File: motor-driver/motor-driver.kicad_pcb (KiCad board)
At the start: 4 copper layers, 155 parts, among them J1 USB_B_Micro, J2 SM03B-SRSS-TB, J3 XT60PW-F, J4 B2B-PH-SM4-TB, Q10 NMOS, Q11 NMOS, Q12 NMOS, Q7 NMOS, Q8 NMOS, Q9 NMOS, SW1 SW_Push, SW2 SW_Push, U1 LM397, U10 W25Q128JVS, U11 DNF, U12 NCP1117-3.3_SOT223, U13 RP2350_80QFN, U2 LM397, U3 LM358DR, U4 LM397, U5 LM358DR, U6 LM358DR, U7 LM358DR, U8 LM358DR, U9 FAN7388, Y1 ABM8-272-T3

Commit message: commit before changing custom sullen key sense
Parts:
- removed the C15 at (219.0, 54.4)
- removed C8: 330uF, 330uFCap:CAPPRD500W60D1000H1400
- removed Q10, Q11, Q12, Q7, Q8, Q9: NMOS, IPD090N03L:DPAK228P998X235-3N
- added C1: 10uF, Capacitor_SMD:C_0603_1608Metric, B.Cu at (181.6, 101.9)
- added C14: 10uF, Capacitor_SMD:C_0603_1608Metric, B.Cu at (181.6, 103.5)
- added C15: 47uF, Capacitor_SMD:C_0603_1608Metric, F.Cu at (133.4, -18.2)
- added C15: 10uF, Capacitor_SMD:C_0603_1608Metric, B.Cu at (181.6, 105.1)
- added C42: 330uF, A768MS337M1VLAS022:CAPAE1030X1225N, B.Cu at (221.3, 60.3)
- added C44: 47uF, Capacitor_SMD:C_0201_0603Metric_Pad0.64x0.40mm_HandSolder, F.Cu at (122.4, -17.7)
- added C44: 10uF, Capacitor_SMD:C_0603_1608Metric, B.Cu at (181.6, 106.7)
- added C45: 10uF, Capacitor_SMD:C_0603_1608Metric, B.Cu at (170.0, 102.1)
- added C46: 10uF, Capacitor_SMD:C_0603_1608Metric, B.Cu at (170.0, 103.6)
- added C47: 10uF, Capacitor_SMD:C_0603_1608Metric, B.Cu at (170.0, 105.2)
- added C48: 10uF, Capacitor_SMD:C_0603_1608Metric, B.Cu at (170.0, 106.7)
- added C49: 10uF, Capacitor_SMD:C_0603_1608Metric, B.Cu at (156.2, 102.1)
- added C50: 10uF, Capacitor_SMD:C_0603_1608Metric, B.Cu at (156.2, 103.6)
- added C51: 10uF, Capacitor_SMD:C_0603_1608Metric, B.Cu at (156.2, 105.2)
- added C52: 10uF, Capacitor_SMD:C_0603_1608Metric, B.Cu at (156.2, 106.7)
- added MOSFET1: AON6512, AON6512:DFN5X6_8L_EP1_P_AOS, B.Cu at (161.7, 105.5)
- added MOSFET2: AON6512, AON6512:DFN5X6_8L_EP1_P_AOS, B.Cu at (156.5, 112.6)
- added MOSFET3: AON6512, AON6512:DFN5X6_8L_EP1_P_AOS, B.Cu at (174.9, 105.5)
- added MOSFET4: AON6512, AON6512:DFN5X6_8L_EP1_P_AOS, B.Cu at (186.4, 105.5)
- added MOSFET5: AON6512, AON6512:DFN5X6_8L_EP1_P_AOS, B.Cu at (169.1, 112.6)
- added MOSFET6: AON6512, AON6512:DFN5X6_8L_EP1_P_AOS, B.Cu at (181.7, 112.6)
- C10, C11, C12, C13, C16, C17, C18, C25, C39, C4, C5, C6, C7, C9: footprint Capacitor_SMD:C_0805_2012Metric -> Capacitor_SMD:C_0603_1608Metric
- C14: footprint Capacitor_SMD:C_0201_0603Metric_Pad0.64x0.40mm_HandSolder -> Capacitor_SMD:C_0603_1608Metric
- C19, C20, C21, C22: footprint Capacitor_SMD:C_0805_2012Metric -> Capacitor_SMD:C_0603_1608Metric; moved to B.Cu
- D1, D2, D3, U1, U2, U4, U9: moved to B.Cu
- R1, R10, R11, R12, R13, R14, R15, R16, R17, R18, R19, R2, R20, R21, R22, R23, R24, R25, R3, R37, R38, R39, R4, R40, R41, R42, R43, R44, R45, R46, R47, R48, R49, R5, R50, R51, R52, R53, R54, R58, R59, R60, R61, R62, R63, R64, R65, R7, R8, R9: footprint Resistor_SMD:R_0805_2012Metric -> Resistor_SMD:R_0603_1608Metric
- R26, R27, R28, R30, R31, R32, R33, R35, R36, R55, R56, R6, R72, R73, R74: footprint Resistor_SMD:R_0805_2012Metric -> Resistor_SMD:R_0603_1608Metric; moved to B.Cu
- moved R74 231.6 mm to (175.6, -67.6)
- moved C22 222.9 mm to (166.2, -69.5), turned to 0 degrees
- moved D3 221.8 mm to (172.1, -67.5)
- moved R72 215.6 mm to (152.3, -53.0), turned to 180 degrees
- moved R73 207.2 mm to (163.0, -44.0), turned to 0 degrees
- moved C19 205.3 mm to (166.6, -51.5), turned to 0 degrees
- moved C21 204.9 mm to (163.2, -51.5), turned to 180 degrees
- moved C20 204.2 mm to (158.6, -51.0), turned to -90 degrees
- moved D1 202.4 mm to (152.2, -49.5), turned to 180 degrees
- moved D2 200.6 mm to (163.1, -47.0), turned to 0 degrees
- moved R54 195.7 mm to (175.3, -52.0)
- moved R28 194.5 mm to (116.9, -36.0), turned to 180 degrees
- moved R41 193.7 mm to (179.9, -40.0), turned to 180 degrees
- moved R26 187.8 mm to (121.4, -36.9), turned to -90 degrees
- moved R43 185.7 mm to (132.4, -44.7), turned to 90 degrees
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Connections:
- J1 pad 1: VBUS -> unconnected-(J1-VBUS-Pad1)
- J4 pad 1: VBUS -> /RP2350/5V
- R59 pad 2: VBUS -> /RP2350/5V
- U12 pad 3: VBUS -> /RP2350/5V
- U3 pad 8: VBUS -> /RP2350/5V
- U5 pad 8: VBUS -> /RP2350/5V
- U6 pad 8: VBUS -> /RP2350/5V
- U7 pad 8: VBUS -> /RP2350/5V
- U8 pad 8: VBUS -> /RP2350/5V
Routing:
- net /current-sensing/W_CURRENT_SENSE_IN: vias 0 -> 4
- net /back-emf-sensing/V_BUS: vias 0 -> 13
- net /back-emf-sensing/MOTOR_GND: vias 0 -> 6
- added copper zone on In2.Cu, net +3V3
- added copper zone on In2.Cu, net /RP2350/5V
- added copper zone on B.Cu, net /back-emf-sensing/MOTOR_GND
- added copper zone on B.Cu, net /back-emf-sensing/U_LEG_COIL
- added copper zone on B.Cu, net /back-emf-sensing/V_BUS
- added copper zone on In2.Cu, net /back-emf-sensing/V_BUS
- added copper zone on B.Cu, net /back-emf-sensing/V_LEG_COIL
- added copper zone on B.Cu, net /back-emf-sensing/W_LEG_COIL
- added copper zone on B.Cu, net /current-sensing/U_CURRENT_SENSE_IN
- added copper zone on F.Cu, net /current-sensing/U_CURRENT_SENSE_IN
- added copper zone on B.Cu, net /current-sensing/V_CURRENT_SENSE_IN
- added copper zone on F.Cu, net /current-sensing/V_CURRENT_SENSE_IN
- added copper zone on B.Cu, net /current-sensing/W_CURRENT_SENSE_IN
- added copper zone on F.Cu, net /current-sensing/W_CURRENT_SENSE_IN
- added copper zone on In1.Cu, net GND
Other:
- board outline added: 40 x 82.4 mm

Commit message: routing complete
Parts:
- removed the C1 at (96.5, 51.2)
- removed the C1 at (181.6, 101.9)
- removed C10, C11, C12, C13, C16, C17, C18, C4, C5, C6, C7, C9: 1nF, Capacitor_SMD:C_0603_1608Metric
- removed the C14 at (144.4, -17.8)
- removed the C14 at (181.6, 103.5)
- removed the C15 at (133.4, -18.2)
- removed the C15 at (181.6, 105.1)
- removed C19: 1uF, Capacitor_SMD:C_0603_1608Metric
- removed C20, C21, C22: 0.1uF, Capacitor_SMD:C_0603_1608Metric
- removed C3: DNF, Capacitor_SMD:C_0402_1005Metric
- removed the C44 at (122.4, -17.7)
- removed the C44 at (181.6, 106.7)
- removed C45, C46, C47, C48, C49, C50, C51, C52: 10uF, Capacitor_SMD:C_0603_1608Metric
- removed D1, D2, D3: D_Schottky, Diode_SMD:D_0805_2012Metric
- removed L1: 100nH, Inductor_SMD:L_0805_2012Metric
- removed MOSFET3, MOSFET4, MOSFET5, MOSFET6: AON6512, AON6512:DFN5X6_8L_EP1_P_AOS
- removed R1, R10, R11, R12, R13, R2, R3, R4, R5, R7, R8, R9: 15k, Resistor_SMD:R_0603_1608Metric
- removed R14, R15, R16, R17, R18, R19: 20k, Resistor_SMD:R_0603_1608Metric
- removed R20, R21, R22, R23, R24, R25, R37, R38, R39, R40, R41, R42, R44, R45, R47, R48, R49, R50, R51, R52, R54, R58, R59, R63, R64, R65: 10k, Resistor_SMD:R_0603_1608Metric
- removed R43, R46, R53: 100k, Resistor_SMD:R_0603_1608Metric
- removed R60, R61, R62: 1k, Resistor_SMD:R_0603_1608Metric
- removed R72, R73, R74: 50, Resistor_SMD:R_0603_1608Metric
- removed R75, R77, R78, R79: DNF, Resistor_SMD:R_0402_1005Metric
- removed SW1, SW2: SW_Push, Button_Switch_SMD:SW_Push_1P1T_NO_Vertical_Wuerth_434133025816
- removed U11: DNF, Package_SO_new:SOIC-8_5.23x5.23mm_P1.27mm
- removed U2, U4: LM397, Package_TO_SOT_SMD:SOT-23-5
- removed U3, U5, U6, U7, U8: LM358DR, LM358DR:SOIC127P599X175-8N
- removed U9: FAN7388, Package_SO:SOIC-20W_7.5x12.8mm_P1.27mm
- added BOOT1: SW_Push, Button_Switch_SMD:SW_Push_1P1T_NO_Vertical_Wuerth_434133025816, F.Cu at (141.5, 59.2)
- added C1: 1uF, Capacitor_SMD:C_0603_1608Metric, F.Cu at (182.6, 83.3)
- added C14: 0.1uF, Capacitor_SMD:C_0603_1608Metric, F.Cu at (183.3, 72.5)
- added C15: 0.1uF, Capacitor_SMD:C_0603_1608Metric, F.Cu at (183.4, 77.9)
- added C43: 10uF, Capacitor_SMD:C_0603_1608Metric, F.Cu at (169.0, 94.2)
- added C44: 0.1uF, Capacitor_SMD:C_0603_1608Metric, F.Cu at (168.2, 81.9)
- added C53: 10uF, Capacitor_SMD:C_0603_1608Metric, F.Cu at (171.2, 94.2)
- added C54: 10uF, Capacitor_SMD:C_0603_1608Metric, F.Cu at (173.3, 94.2)
- added C55: 10uF, Capacitor_SMD:C_0603_1608Metric, F.Cu at (148.9, 93.9)
- added C56: 10uF, Capacitor_SMD:C_0603_1608Metric, F.Cu at (151.2, 93.9)
- added C57: 10uF, Capacitor_SMD:C_0603_1608Metric, F.Cu at (153.5, 93.9)
- added C58: 10uF, Capacitor_SMD:C_0603_1608Metric, F.Cu at (155.8, 93.9)
- added C59: 10uF, Capacitor_SMD:C_0603_1608Metric, F.Cu at (184.7, 93.8)
- added C60: 10uF, Capacitor_SMD:C_0603_1608Metric, F.Cu at (186.9, 93.8)
- added C61: 10uF, Capacitor_SMD:C_0603_1608Metric, F.Cu at (189.0, 93.8)
- added C62: 10uF, Capacitor_SMD:C_0603_1608Metric, F.Cu at (191.2, 93.8)
- added C8: 10uF, Capacitor_SMD:C_0603_1608Metric, F.Cu at (166.8, 94.2)
- added C_bypass1: 0.1uF, Capacitor_SMD:C_0603_1608Metric, F.Cu at (141.7, 101.2)
- added C_bypass2: 0.1uF, Capacitor_SMD:C_0603_1608Metric, F.Cu at (159.8, 101.5)
- added C_bypass3: 0.1uF, Capacitor_SMD:C_0603_1608Metric, F.Cu at (177.6, 101.5)
- added D4: D_Schottky, Diode_SMD:D_0805_2012Metric, F.Cu at (183.4, 69.1)
- added D5: D_Schottky, Diode_SMD:D_0805_2012Metric, F.Cu at (186.3, 77.1)
- added D6: D_Schottky, Diode_SMD:D_0805_2012Metric, F.Cu at (169.7, 84.9)
- added MOSFET10: AON6512, AON6512:DFN5X6_8L_EP1_P_AOS, F.Cu at (182.6, 101.8)
- added MOSFET7: AON6512, AON6512:DFN5X6_8L_EP1_P_AOS, F.Cu at (171.3, 101.8)
- added MOSFET8: AON6512, AON6512:DFN5X6_8L_EP1_P_AOS, F.Cu at (164.8, 101.8)
- added MOSFET9: AON6512, AON6512:DFN5X6_8L_EP1_P_AOS, F.Cu at (189.0, 101.8)
- added R100: 50, Resistor_SMD:R_0603_1608Metric, F.Cu at (169.8, 87.1)
- added R66: 22, Resistor_SMD:R_0603_1608Metric, F.Cu at (160.7, 96.3)
- added R67: 22, Resistor_SMD:R_0603_1608Metric, B.Cu at (173.4, 103.7)
- added R68: 10k, Resistor_SMD:R_0603_1608Metric, F.Cu at (173.4, 107.7)
- added R69: 10k, Resistor_SMD:R_0603_1608Metric, F.Cu at (159.8, 99.0)
- added R70: 5m, Resistor_SMD:R_2512_6332Metric, F.Cu at (164.1, 110.1)
- added R71: 22, Resistor_SMD:R_0603_1608Metric, F.Cu at (178.3, 96.3)
- added R86: 22, Resistor_SMD:R_0603_1608Metric, B.Cu at (190.8, 103.7)
- added R87: 10k, Resistor_SMD:R_0603_1608Metric, F.Cu at (191.4, 107.1)
- added R88: 10k, Resistor_SMD:R_0603_1608Metric, F.Cu at (177.8, 99.2)
- added R89: 5m, Resistor_SMD:R_2512_6332Metric, F.Cu at (182.2, 110.1)
- added R90: 10k, Resistor_SMD:R_0603_1608Metric, F.Cu at (159.6, 86.7)
- added R91: 10k, Resistor_SMD:R_0603_1608Metric, F.Cu at (163.5, 85.8)
- added R92: 10k, Resistor_SMD:R_0603_1608Metric, F.Cu at (158.4, 83.2)
- added R93: 1M, Resistor_SMD:R_0603_1608Metric, F.Cu at (164.2, 82.9)
- added R94: 10k, Resistor_SMD:R_0603_1608Metric, F.Cu at (163.2, 79.8)
- added R95: 10k, Resistor_SMD:R_0603_1608Metric, B.Cu at (149.6, 88.5)
- added R96: 10k, Resistor_SMD:R_0603_1608Metric, B.Cu at (151.2, 88.5)
- added R97: 10k, Resistor_SMD:R_0603_1608Metric, B.Cu at (152.8, 88.5)
- added R98: 50, Resistor_SMD:R_0603_1608Metric, F.Cu at (181.2, 68.7)
- added R99: 50, Resistor_SMD:R_0603_1608Metric, F.Cu at (186.4, 78.9)
- added RUN1: SW_Push, Button_Switch_SMD:SW_Push_1P1T_NO_Vertical_Wuerth_434133025816, F.Cu at (141.5, 66.9)
- added U14: LM397, Package_TO_SOT_SMD:SOT-23-5, F.Cu at (144.2, 83.4)
- added U15: LM397, Package_TO_SOT_SMD:SOT-23-5, F.Cu at (152.7, 83.0)
- added U16: LM397, Package_TO_SOT_SMD:SOT-23-5, F.Cu at (161.4, 82.9)
- added U17: FAN7388, Package_SO:SOIC-20W_7.5x12.8mm_P1.27mm, F.Cu at (175.8, 77.1)
- added U19: INA240A1PWR, INA240A1PWR:SOP65P640X120-8N, F.Cu at (141.5, 106.5)
- added U20: INA240A1PWR, INA240A1PWR:SOP65P640X120-8N, F.Cu at (159.5, 106.5)
- added U21: INA240A1PWR, INA240A1PWR:SOP65P640X120-8N, F.Cu at (177.6, 106.5)
- added V1: PAD, TestPoint:TestPoint_Pad_4.0x4.0mm, F.Cu at (169.3, 113.1)
- added W1: PAD, TestPoint:TestPoint_Pad_4.0x4.0mm, F.Cu at (187.4, 113.1)
- C26, C27: footprint Capacitor_SMD:C_0603_1608Metric -> Capacitor_SMD:C_0402_1005Metric
- C42, MOSFET1, MOSFET2, R27, R28, R30, R35: moved to F.Cu
- L2: footprint Inductor_SMD:L_0603_1608Metric -> Inductor_SMD:L_Cenker_CKCS201610
- R26, R31, R32, R36, R55: value 22 -> 10k; moved to F.Cu
- R33, R56: value 10k -> 1M; moved to F.Cu
- R34, R57: value 5m -> 10k; footprint Resistor_SMD:R_2512_6332Metric -> Resistor_SMD:R_0603_1608Metric
- R6: value 10k -> 22
- U1: value LM397 -> PAD; footprint Package_TO_SOT_SMD:SOT-23-5 -> TestPoint:TestPoint_Pad_4.0x4.0mm; moved to F.Cu
- moved H1 247.5 mm to (262.0, 86.5)
- moved H2 247.5 mm to (262.0, 93.4)
- moved H3 247.5 mm to (262.0, 100.3)
- moved H4 247.5 mm to (262.0, 107.3)
- moved J2 154.6 mm to (162.2, 73.1), turned to 0 degrees
- moved R26 148.2 mm to (155.6, 107.3), turned to 90 degrees
- moved R6 140.0 mm to (155.4, 103.3), turned to -90 degrees
- moved R28 137.3 mm to (141.8, 99.0), turned to 0 degrees
- moved R27 133.1 mm to (142.7, 96.3)
- moved R35 127.3 mm to (151.2, 86.9), turned to -90 degrees
- moved R30 124.4 mm to (142.4, 87.1), turned to -90 degrees
- moved R55 124.2 mm to (149.8, 83.6), turned to 90 degrees
- moved R36 124.0 mm to (154.6, 86.0), turned to 180 degrees
- moved R31 123.7 mm to (146.2, 86.3), turned to 180 degrees
- moved R32 122.0 mm to (141.4, 83.7), turned to 90 degrees
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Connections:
- C2 pad 1: +3V3 -> 3V3
- C25 pad 1: +3V3 -> 3V3
- C26 pad 1: +3V3 -> 3V3
- C32 pad 1: +3V3 -> 3V3
- C33 pad 1: +3V3 -> 3V3
- C34 pad 1: +3V3 -> 3V3
- C35 pad 1: +3V3 -> 3V3
- C36 pad 1: +3V3 -> 3V3
- C37 pad 1: +3V3 -> 3V3
- C38 pad 1: +3V3 -> 3V3
- C39 pad 1: +3V3 -> 3V3
- C40 pad 1: +3V3 -> 3V3
- C41 pad 1: +3V3 -> 3V3
- C42 pad 1: /back-emf-sensing/V_BUS -> V_BUS
- C42 pad 2: /back-emf-sensing/MOTOR_GND -> GND
- J1 pad 1: unconnected-(J1-VBUS-Pad1) -> 5V
- J3 pad 1: /back-emf-sensing/V_BUS -> V_BUS
- J3 pad 2: /back-emf-sensing/MOTOR_GND -> GND
- J4 pad 1: /RP2350/5V -> 5V
- J4 pad 2: /back-emf-sensing/MOTOR_GND -> GND
- MOSFET1 pad 1: /back-emf-sensing/U_LEG_COIL -> /inverter/inverter_u/SHUNT_P
- MOSFET1 pad 2: /back-emf-sensing/U_LEG_COIL -> /inverter/inverter_u/SHUNT_P
- MOSFET1 pad 3: /back-emf-sensing/U_LEG_COIL -> /inverter/inverter_u/SHUNT_P
- MOSFET1 pad 5: /back-emf-sensing/V_BUS -> V_BUS
- MOSFET1 pad 6: /back-emf-sensing/V_BUS -> V_BUS
- MOSFET1 pad 7: /back-emf-sensing/V_BUS -> V_BUS
- MOSFET1 pad 8: /back-emf-sensing/V_BUS -> V_BUS
- MOSFET2 pad 1: /current-sensing/U_CURRENT_SENSE_IN -> GND
- MOSFET2 pad 2: /current-sensing/U_CURRENT_SENSE_IN -> GND
- MOSFET2 pad 3: /current-sensing/U_CURRENT_SENSE_IN -> GND
- MOSFET2 pad 5: /back-emf-sensing/U_LEG_COIL -> /inverter/inverter_u/SHUNT_P
- MOSFET2 pad 6: /back-emf-sensing/U_LEG_COIL -> /inverter/inverter_u/SHUNT_P
- MOSFET2 pad 7: /back-emf-sensing/U_LEG_COIL -> /inverter/inverter_u/SHUNT_P
- MOSFET2 pad 8: /back-emf-sensing/U_LEG_COIL -> /inverter/inverter_u/SHUNT_P
- R26 pad 1: /gate-driver/U_LEG_HIGH -> GND
- R27 pad 1: /gate-driver/U_LEG_LOW -> /inverter/gate-driver/U_GATE_L
- R28 pad 1: /back-emf-sensing/MOTOR_GND -> GND
- R28 pad 2: Net-(MOSFET1-Pad4) -> Net-(MOSFET2-Pad4)
- R29 pad 1: /back-emf-sensing/MOTOR_GND -> /inverter/inverter_u/SHUNT_N
- R29 pad 2: /current-sensing/U_CURRENT_SENSE_IN -> /inverter/inverter_u/SHUNT_P
- R30 pad 1: /back-emf-sensing/MOTOR_GND -> Net-(U14--)
- R30 pad 2: Net-(MOSFET5-Pad4) -> /inverter/inverter_u/SHUNT_N
- R31 pad 1: /gate-driver/V_LEG_HIGH -> GND
- R31 pad 2: Net-(MOSFET3-Pad4) -> MOTOR_NEUTRAL_REF
- R32 pad 1: /inverter/V_LEG_LOW -> Net-(U14--)
- R32 pad 2: Net-(MOSFET5-Pad4) -> GND
- R33 pad 1: /back-emf-sensing/MOTOR_GND -> MOTOR_NEUTRAL_REF
- R33 pad 2: Net-(MOSFET3-Pad4) -> /RP2350/BACK_EMF_U
- R34 pad 1: /back-emf-sensing/MOTOR_GND -> 3V3
- R34 pad 2: /current-sensing/V_CURRENT_SENSE_IN -> /RP2350/BACK_EMF_U
- R35 pad 1: /back-emf-sensing/MOTOR_GND -> Net-(U15--)
- R35 pad 2: Net-(MOSFET6-Pad4) -> /inverter/inverter_v/SHUNT_N
- R36 pad 1: /gate-driver/W_LEG_HIGH -> GND
- R36 pad 2: Net-(MOSFET4-Pad4) -> MOTOR_NEUTRAL_REF
- R55 pad 1: /gate-driver/W_LEG_LOW -> Net-(U15--)
- R55 pad 2: Net-(MOSFET6-Pad4) -> GND
- R56 pad 1: /back-emf-sensing/MOTOR_GND -> MOTOR_NEUTRAL_REF
- R56 pad 2: Net-(MOSFET4-Pad4) -> /RP2350/BACK_EMF_V
- R57 pad 1: /back-emf-sensing/MOTOR_GND -> 3V3
- R57 pad 2: /current-sensing/W_CURRENT_SENSE_IN -> /RP2350/BACK_EMF_V
- R6 pad 1: /back-emf-sensing/MOTOR_GND -> /inverter/gate-driver/U_GATE_H
- R6 pad 2: Net-(MOSFET2-Pad4) -> Net-(MOSFET1-Pad4)
- R82 pad 1: +3V3 -> 3V3
- U1 pad 1: Net-(U1--) -> /inverter/inverter_u/SHUNT_N
- U10 pad 8: +3V3 -> 3V3
- U12 pad 2: +3V3 -> 3V3
- U12 pad 3: /RP2350/5V -> 5V
- U13 pad 1: /RP2350/PWM_U_H -> unconnected-(U13-GPIO4-Pad1)
- U13 pad 11: /RP2350/GPIO10 -> /RP2350/GPIO12
- U13 pad 12: /RP2350/GPIO10 -> /RP2350/GPIO13
- U13 pad 13: /RP2350/GPIO10 -> /RP2350/GPIO14
- U13 pad 14: /RP2350/GPIO10 -> /RP2350/GPIO15
- U13 pad 15: +3V3 -> 3V3
- U13 pad 16: /RP2350/GPIO10 -> /RP2350/GPIO16
- U13 pad 17: /RP2350/GPIO10 -> /RP2350/GPIO17
- U13 pad 18: /RP2350/GPIO10 -> /RP2350/GPIO18
- U13 pad 19: /RP2350/GPIO10 -> /RP2350/GPIO19
- U13 pad 2: /RP2350/PWM_U_L -> unconnected-(U13-GPIO5-Pad2)
- U13 pad 20: /RP2350/GPIO10 -> /RP2350/GPIO20
- U13 pad 21: /RP2350/GPIO10 -> /RP2350/BACK_EMF_U
- U13 pad 22: /RP2350/GPIO10 -> /RP2350/BACK_EMF_V
- U13 pad 23: /RP2350/GPIO10 -> /RP2350/BACK_EMF_W
- U13 pad 24: +3V3 -> 3V3
- U13 pad 25: /RP2350/GPIO10 -> /RP2350/GPIO24
- U13 pad 26: /RP2350/GPIO10 -> /RP2350/GPIO25
- U13 pad 27: /RP2350/GPIO10 -> /RP2350/GPIO26
- U13 pad 28: /RP2350/GPIO10 -> /RP2350/GPIO27
- U13 pad 29: +3V3 -> 3V3
- U13 pad 3: /RP2350/PWM_V_H -> unconnected-(U13-GPIO6-Pad3)
- U13 pad 36: /RP2350/GPIO10 -> /RP2350/PWM_U_L
- U13 pad 37: /RP2350/GPIO10 -> /RP2350/PWM_U_H
- U13 pad 38: /RP2350/GPIO10 -> /RP2350/PWM_V_L
- U13 pad 39: /RP2350/GPIO10 -> /RP2350/PWM_V_H
- U13 pad 4: /RP2350/PWM_V_L -> unconnected-(U13-GPIO7-Pad4)
- U13 pad 40: /RP2350/GPIO10 -> /RP2350/PWM_W_L
- U13 pad 41: +3V3 -> 3V3
- U13 pad 42: /RP2350/GPIO10 -> /RP2350/PWM_W_H
- U13 pad 43: /RP2350/GPIO10 -> /RP2350/GPIO34
- U13 pad 44: /RP2350/GPIO10 -> /RP2350/GPIO35
- U13 pad 45: /RP2350/GPIO10 -> /RP2350/GPIO36
- U13 pad 46: /RP2350/GPIO10 -> /RP2350/GPIO37
- U13 pad 47: /RP2350/GPIO10 -> /RP2350/GPIO38
- U13 pad 48: /RP2350/GPIO10 -> /RP2350/GPIO39
- U13 pad 49: /RP2350/CURRENT_SENSE_U -> unconnected-(U13-GPIO40_ADC0-Pad49)
- U13 pad 5: +3V3 -> 3V3
- U13 pad 50: +3V3 -> 3V3
- U13 pad 52: /RP2350/CURRENT_SENSE_V -> unconnected-(U13-GPIO41_ADC1-Pad52)
- U13 pad 53: /RP2350/CURRENT_SENSE_W -> unconnected-(U13-GPIO42_ADC2-Pad53)
- U13 pad 55: /RP2350/GPIO43_ADC3 -> /RP2350/CURRENT_SENSE_U
- U13 pad 56: /RP2350/GPIO43_ADC3 -> /RP2350/CURRENT_SENSE_V
- U13 pad 57: /RP2350/GPIO43_ADC3 -> /RP2350/CURRENT_SENSE_W
- U13 pad 58: /RP2350/GPIO43_ADC3 -> /RP2350/GPIO47_ADC7
- U13 pad 59: +3V3 -> 3V3
- U13 pad 6: /RP2350/PWM_W_H -> unconnected-(U13-GPIO8-Pad6)
- U13 pad 60: +3V3 -> 3V3
- U13 pad 64: +3V3 -> 3V3
- U13 pad 68: +3V3 -> 3V3
- U13 pad 69: +3V3 -> 3V3
- U13 pad 7: /RP2350/PWM_W_L -> unconnected-(U13-GPIO9-Pad7)
- U13 pad 76: +3V3 -> 3V3
- U13 pad 77: /RP2350/BACK_EMF_U -> unconnected-(U13-GPIO0-Pad77)
- U13 pad 78: /RP2350/BACK_EMF_V -> unconnected-(U13-GPIO1-Pad78)
- U13 pad 79: /RP2350/BACK_EMF_W -> unconnected-(U13-GPIO2-Pad79)
- U13 pad 9: /RP2350/GPIO10 -> /RP2350/GPIO11
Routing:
- net /inverter/inverter_w/SHUNT_N: track 0.00 -> 86.4 mm, vias 0 -> 2
- net /inverter/inverter_v/SHUNT_N: track 0.00 -> 67.8 mm, vias 0 -> 4
- net GND: track 0.00 -> 67.4 mm, vias 0 -> 90
- net /RP2350/CURRENT_SENSE_U: track 0.00 -> 62.6 mm, vias 0 -> 2
- net 3V3: track 0.00 -> 61.4 mm, vias 0 -> 18
- net /inverter/inverter_u/SHUNT_P: track 0.00 -> 57.5 mm, vias 0 -> 2
- net /RP2350/CURRENT_SENSE_W: track 0.00 -> 57.2 mm
- net /inverter/inverter_w/SHUNT_P: track 0.00 -> 57.0 mm, vias 0 -> 2
- net /inverter/inverter_v/SHUNT_P: track 0.00 -> 55.7 mm, vias 0 -> 2
- net /RP2350/CURRENT_SENSE_V: track 0.00 -> 50.4 mm, vias 0 -> 2
- net /inverter/inverter_u/SHUNT_N: track 0.00 -> 47.6 mm, vias 0 -> 2
- net /inverter/gate-driver/W_GATE_H: track 0.00 -> 40.4 mm, vias 0 -> 1
- net /inverter/gate-driver/U_GATE_L: track 0.00 -> 38.2 mm, vias 0 -> 2
- net /inverter/gate-driver/V_GATE_L: track 0.00 -> 37.7 mm, vias 0 -> 2
- net /RP2350/BACK_EMF_W: track 0.00 -> 34.8 mm
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- added copper zone on F.Cu, net +1V1
- added copper zone on F.Cu, net /RP2350/USB_D+
- added copper zone on F.Cu, net /RP2350/USB_D-
- added copper zone on F.Cu, net /RP2350/VREG_LX
- added copper zone on F.Cu, net /inverter/inverter_u/SHUNT_N
- added copper zone on F.Cu, net /inverter/inverter_u/SHUNT_P
- added copper zone on F.Cu, net /inverter/inverter_v/SHUNT_N
- added copper zone on F.Cu, net /inverter/inverter_v/SHUNT_P
- added copper zone on F.Cu, net /inverter/inverter_w/SHUNT_N
- added copper zone on F.Cu, net /inverter/inverter_w/SHUNT_P
- added copper zone on F.Cu, net 3V3
- added copper zone on In2.Cu, net 3V3
- added copper zone on F.Cu, net 5V
- added copper zone on F.Cu, net GND
- added copper zone on F.Cu, net V_BUS
- added copper zone on In2.Cu, net V_BUS
- removed copper zone on In2.Cu, net +3V3
- removed copper zone on In2.Cu, net /RP2350/5V
- removed copper zone on B.Cu, net /back-emf-sensing/MOTOR_GND
- removed copper zone on B.Cu, net /back-emf-sensing/U_LEG_COIL
- removed copper zone on B.Cu, net /back-emf-sensing/V_BUS
- removed copper zone on In2.Cu, net /back-emf-sensing/V_BUS
- removed copper zone on B.Cu, net /back-emf-sensing/V_LEG_COIL
- removed copper zone on B.Cu, net /back-emf-sensing/W_LEG_COIL
- removed copper zone on B.Cu, net /current-sensing/U_CURRENT_SENSE_IN
- removed copper zone on F.Cu, net /current-sensing/U_CURRENT_SENSE_IN
- removed copper zone on B.Cu, net /current-sensing/V_CURRENT_SENSE_IN
- removed copper zone on F.Cu, net /current-sensing/V_CURRENT_SENSE_IN
- removed copper zone on B.Cu, net /current-sensing/W_CURRENT_SENSE_IN
- removed copper zone on F.Cu, net /current-sensing/W_CURRENT_SENSE_IN
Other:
- board size 40 x 82.4 mm -> 56 x 85.4 mm

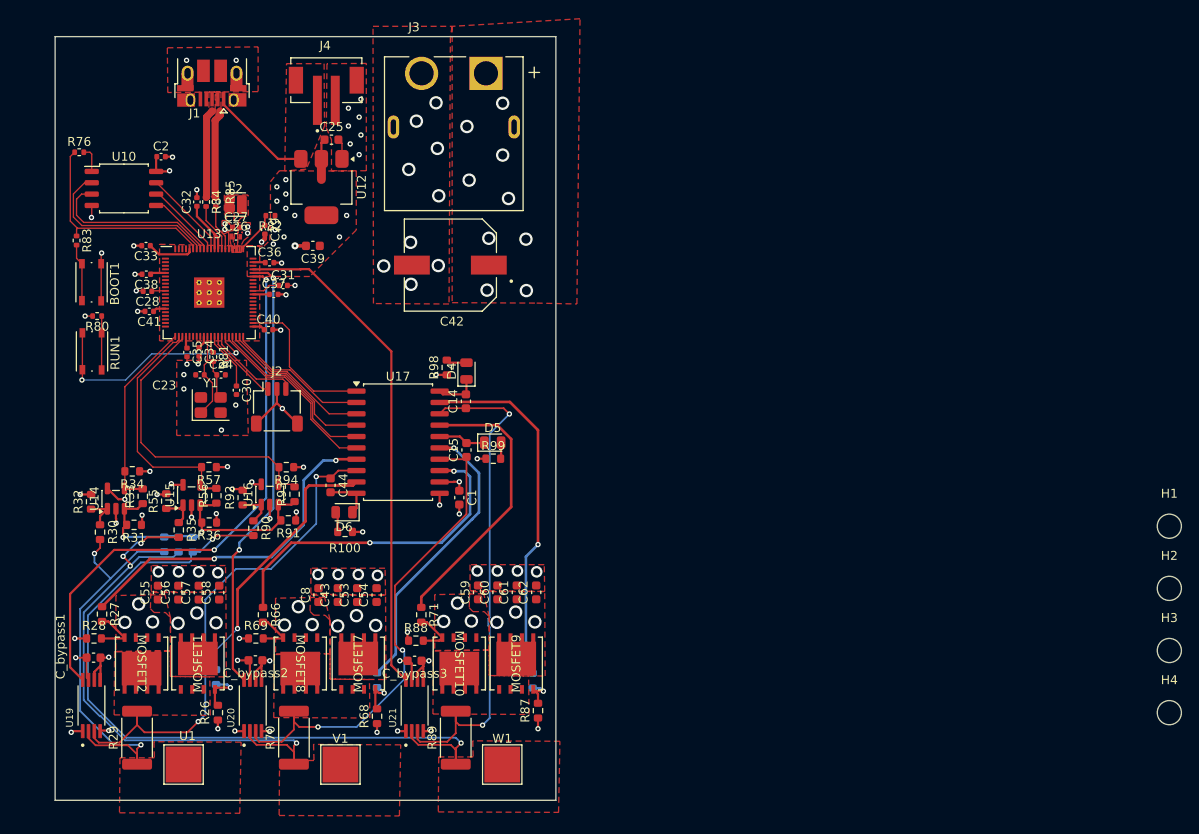
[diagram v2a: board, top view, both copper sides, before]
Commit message: added spi connection
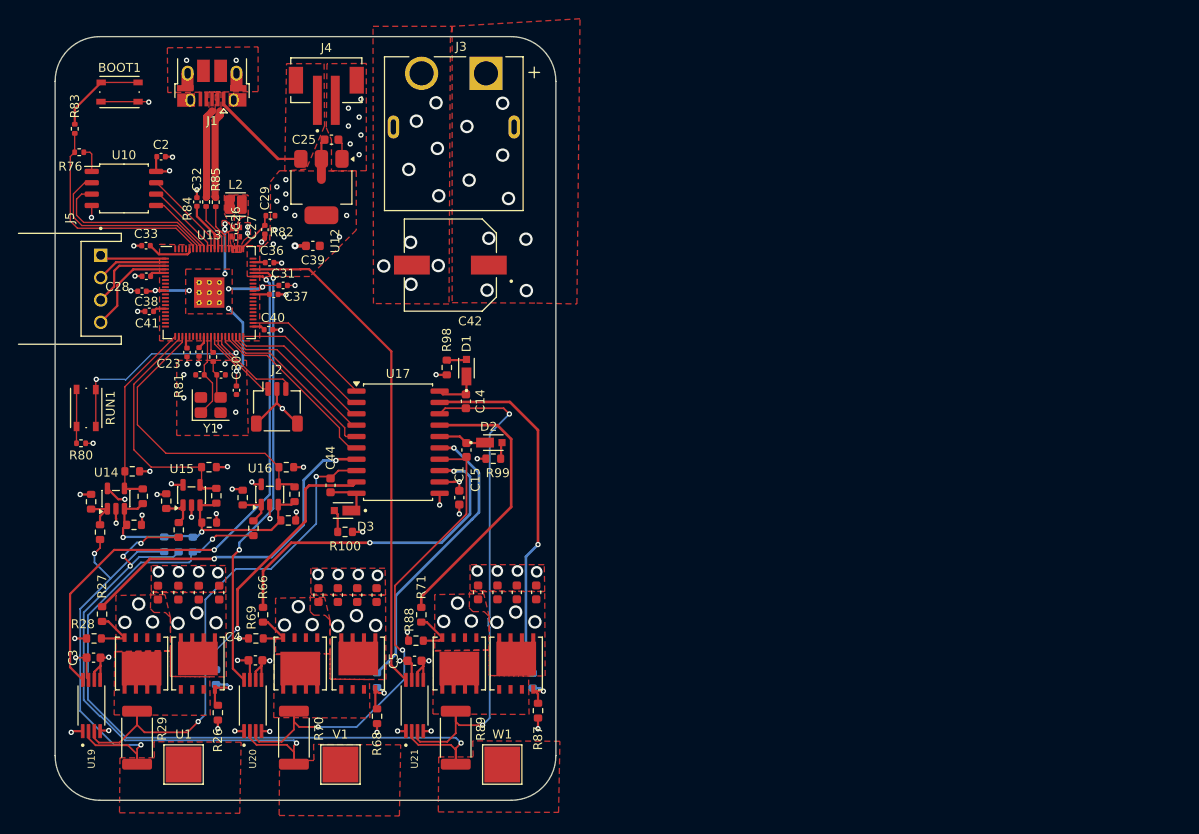
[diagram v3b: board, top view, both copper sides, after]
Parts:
- removed D4, D5, D6: D_Schottky, Diode_SMD:D_0805_2012Metric
- removed H1, H2, H3, H4: MountingHole, MountingHole:MountingHole_2.7mm_M2.5
- added D1: MSS1P6-M3_89A, MSS1P6-M3_89A:DIO_MSS1P6-M3_89A, F.Cu at (183.4, 68.8)
- added D2: MSS1P6-M3_89A, MSS1P6-M3_89A:DIO_MSS1P6-M3_89A, F.Cu at (186.4, 77.1)
- added D3: MSS1P6-M3_89A, MSS1P6-M3_89A:DIO_MSS1P6-M3_89A, F.Cu at (169.6, 84.7)
- added J5: S4B-XH-A, S4B-XH-A:JST_S4B-XH-A, F.Cu at (136.8, 59.9)
- BOOT1, RUN1: value SW_Push -> 434133025816
- C43, C53, C54, C55, C56, C57, C58, C59, C60, C61, C62, C8: value 10uF -> GRM188R6YA106MA73D
- J1: value USB_B_Micro -> 10103594-0001LF
- L2: value 3.3u -> AOTA-B201610S3R3-101-T
- U12: value NCP1117-3.3_SOT223 -> NCP1117ST33T3G
- U13: value RP2350_80QFN -> RP2350B
- moved BOOT1 21.5 mm to (144.6, 37.9), turned to 180 degrees
- moved R80 14.3 mm to (140.3, 77.2), turned to 0 degrees
- moved R83 12.5 mm to (139.6, 42.0), turned to 90 degrees
- moved RUN1 6.36 mm to (140.9, 73.2), turned to 90 degrees
- moved C28 0.61 mm to (147.1, 60.2)
- moved C38 0.23 mm to (147.6, 58.5)
- renumbered C_bypass1 to C3, C_bypass2 to C4, C_bypass3 to C5
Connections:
- U13 pad 1: unconnected-(U13-GPIO4-Pad1) -> /RP2350/MOSI
- U13 pad 2: unconnected-(U13-GPIO5-Pad2) -> /RP2350/CS
- U13 pad 3: unconnected-(U13-GPIO6-Pad3) -> /RP2350/SCLK
- U13 pad 4: unconnected-(U13-GPIO7-Pad4) -> /RP2350/MISO
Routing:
- net +1V1: track 13.5 -> 35.5 mm, vias 2 -> 9
- net /RP2350/MISO: track 0.00 -> 11.0 mm
- net /RP2350/SCLK: track 0.00 -> 9.85 mm
- net /RP2350/CS: track 0.00 -> 7.95 mm
- net /RP2350/MOSI: track 0.00 -> 7.39 mm
- net /RP2350/~{USB_BOOT}: track 6.46 -> 10.0 mm
- net /RP2350/PWM_W_H: track 17.1 -> 14.7 mm
- net /RP2350/RUN: track 26.1 -> 24.6 mm
- net /RP2350/QSPI_SS: track 24.1 -> 25.3 mm
- net /RP2350/PWM_V_L: track 18.6 -> 17.8 mm
- net /RP2350/BACK_EMF_W: track 34.8 -> 34.2 mm
- net /RP2350/PWM_U_H: track 20.1 -> 19.5 mm
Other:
- outline, holes or cut-outs redrawn

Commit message: board ready for review
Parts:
- moved J1 1.74 mm to (154.5, 35.2)
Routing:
- net /RP2350/USB_D+: track 9.95 -> 12.9 mm
- net /RP2350/USB_D-: track 9.96 -> 12.8 mm
- net 5V: track 11.8 -> 13.3 mm
- removed copper zone on F.Cu, net /RP2350/USB_D+
- removed copper zone on F.Cu, net /RP2350/USB_D-
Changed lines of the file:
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@@
 	(footprint "Connector_USB:USB_Micro-B_Amphenol_10103594-0001LF_Horizontal"
 		(layer "F.Cu")
-		(at 154.924178 36.909653 180)
+		(at 154.525 35.215 180)
 		(descr "Micro USB Type B 10103594-0001LF, http://cdn.amphenol-icc.com/media/wysiwyg/files/drawing/10103594.pdf")
 		(tags "USB USB_B USB_micro USB_OTG")
@@
 	)
 	(via
-		(at 152.1 34.35)
+		(at 151.725 32.55)
 		(size 0.6)
 		(drill 0.3)
@@
 	)
 	(via
-		(at 157.65 34.35)
+		(at 157.225 32.525)
 		(size 0.6)
 		(drill 0.3)
@@
 	)
 	(segment
+		(start 155.125 39.215936)
+		(end 155.125 38.292501)
+		(width 0.3)
+		(layer "F.Cu")
+		(net 6)
+	)
+	(segment
+		(start 155.2 38.217501)
+		(end 155.2 36.98)
+		(width 0.3)
+		(layer "F.Cu")
+		(net 6)
+	)
+	(segment
+		(start 155.291011 39.381947)
+		(end 155.125 39.215936)
+		(width 0.3)
+		(layer "F.Cu")
+		(net 6)
+	)
+	(segment
 		(start 155.366011 49.697986)
 		(end 155.291011 49.622986)
@@
 	)
 	(segment
-		(start 155.291011 49.622986)
-		(end 155.291011 41.073059)
-		(width 0.8)
+		(start 155.125 38.292501)
+		(end 155.2 38.217501)
+		(width 0.3)
 		(layer "F.Cu")
 		(net 6)
 	)
 	(segment
-		(start 155.291011 41.073059)
-		(end 155.850178 40.513892)
+		(start 155.291011 49.622986)
+		(end 155.291011 39.381947)
 		(width 0.8)
 		(layer "F.Cu")
@@
 	)
 	(segment
-		(start 155.850178 40.513892)
-		(end 155.850177 40.000653)
-		(width 0.8)
+		(start 154.341011 38.988443)
+		(end 154.625 38.704454)
+		(width 0.3)
 		(layer "F.Cu")
-		(net 6)
+		(net 8)
 	)
 	(segment
@@
 	)
 	(segment
-		(start 154.949178 40.071388)
-		(end 154.949178 40.000653)
+		(start 154.341011 49.622986)
+		(end 154.341011 38.988443)
 		(width 0.8)
 		(layer "F.Cu")
@@
 	)
 	(segment
-		(start 154.341011 40.679555)
-		(end 154.949178 40.071388)
-		(width 0.8)
+		(start 154.625 38.292501)
+		(end 154.55 38.217501)
+		(width 0.3)
 		(layer "F.Cu")
 		(net 8)
 	)
 	(segment
-		(start 154.341011 49.622986)
-		(end 154.341011 40.679555)
-		(width 0.8)
+		(start 154.55 38.217501)
+		(end 154.55 36.98)
+		(width 0.3)
+		(layer "F.Cu")
+		(net 8)
+	)
+	(segment
+		(start 154.625 38.704454)
+		(end 154.625 38.292501)
+		(width 0.3)
 		(layer "F.Cu")
 		(net 8)
@@
 	)
 	(segment
-		(start 162.324178 45.374653)
+		(start 162.924653 45.374653)
 		(end 164.879178 45.374653)
-		(width 0.25)
+		(width 0.6)
 		(layer "F.Cu")
 		(net 43)
 	)
 	(segment
-		(start 156.249178 39.299653)
-		(end 162.324178 45.374653)
-		(width 0.35)
+		(start 155.85 38.3)
+		(end 162.924653 45.374653)
+		(width 0.6)
 		(layer "F.Cu")
 		(net 43)
 	)
 	(segment
-		(start 156.249178 38.674653)
-		(end 156.249178 39.299653)
-		(width 0.25)
+		(start 155.85 36.98)
+		(end 155.85 38.3)
+		(width 0.6)
 		(layer "F.Cu")
 		(net 43)
@@
 	)
 	(segment
-		(start 144.351 61.799)
-		(end 142.5 63.65)
+		(start 146.135301 57.724653)
+		(end 144.6 59.259954)
 		(width 0.25)
 		(layer "F.Cu")
@@
 	)
 	(segment
-		(start 146.135301 57.724653)
-		(end 144.351 59.508954)
+		(start 144.6 59.259954)
+		(end 144.6 61.55)
 		(width 0.25)
 		(layer "F.Cu")
@@
 	)
 	(segment
-		(start 144.351 59.508954)
-		(end 144.351 61.799)
+		(start 144.6 61.55)
+		(end 142.5 63.65)
 		(width 0.25)
 		(layer "F.Cu")
@@
 	)
 	(zone
-		(net 8)
-		(net_name "/RP2350/USB_D+")
-		(layer "F.Cu")
-		(hatch edge 0.5)
-		(priority 10)
-		(connect_pads yes
-			(clearance 0.01)
-		)
-		(min_thickness 0.025)
-		(filled_areas_thickness no)
-		(fill yes
-			(thermal_gap 0.5)
-			(thermal_bridge_width 0.5)
-		)
-		(polygon
-			(pts
-				(xy 154.6 37.9) (xy 154.6 39.9) (xy 155.3 39.9) (xy 155.3 37.9)
-			)
-		)
-	)
-	(zone
 		(net 0)
 		(net_name "")
@@
 		(polygon
 			(pts
-				(xy 149.95 32.95) (xy 160.1 32.85) (xy 160.1 37.85) (xy 150 37.95)
+				(xy 150.35 31.2) (xy 158.95 31.275) (xy 158.9 36.774711) (xy 150.363465 36.859232)
 			)
 		)
@@
 			)
 		)
-	)
-	(zone
-		(net 6)
-		(net_name "/RP2350/USB_D-")
-		(layer "F.Cu")
-		(hatch edge 0.5)
-		(priority 11)
-		(connect_pads yes
-			(clearance 0.01)
-		)
-		(min_thickness 0.025)
-		(filled_areas_thickness no)
-		(fill yes
-			(thermal_gap 0.5)
-			(thermal_bridge_width 0.5)
-		)
-		(polygon
-			(pts
-				(xy 155.4 37.9) (xy 155.95 37.9) (xy 155.95 40.5) (xy 155.4 40.5)
-			)
-		)

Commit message: added test points
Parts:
- added 3V3: TestPoint, TestPoint:TestPoint_THTPad_D1.0mm_Drill0.5mm, F.Cu at (171.1, 56.4)
- added 5V1: TestPoint, TestPoint:TestPoint_THTPad_D1.0mm_Drill0.5mm, F.Cu at (161.3, 40.8)
- added BEMFU1: TestPoint, TestPoint:TestPoint_THTPad_D1.0mm_Drill0.5mm, F.Cu at (141.0, 78.2)
- added GND1: TestPoint, TestPoint:TestPoint_THTPad_D1.0mm_Drill0.5mm, F.Cu at (174.8, 63.4)
- added NEUTRAL1: TestPoint, TestPoint:TestPoint_THTPad_D1.0mm_Drill0.5mm, F.Cu at (139.9, 87.6)
- added SENSEW1: TestPoint, TestPoint:TestPoint_THTPad_D1.0mm_Drill0.5mm, F.Cu at (167.3, 62.6)
- added VBUS1: TestPoint, TestPoint:TestPoint_THTPad_D1.0mm_Drill0.5mm, F.Cu at (188.4, 63.6)
- added WGATE_BST1: TestPoint, TestPoint:TestPoint_THTPad_D1.0mm_Drill0.5mm, F.Cu at (189.8, 77.1)
- added WGATE_H1: TestPoint, TestPoint:TestPoint_THTPad_D1.0mm_Drill0.5mm, F.Cu at (189.3, 87.3)
- moved R80 3.08 mm to (140.3, 74.1)
- moved RUN1 3.07 mm to (140.9, 70.2)
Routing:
- net MOTOR_NEUTRAL_REF: track 33.3 -> 38.5 mm
- net /RP2350/BACK_EMF_U: track 21.7 -> 26.3 mm
- net /inverter/inverter_w/SHUNT_P: track 57.0 -> 60.8 mm
- net 3V3: track 61.4 -> 64.4 mm
- net /RP2350/CURRENT_SENSE_W: track 57.2 -> 59.6 mm
- net 5V: track 13.3 -> 15.5 mm
- net /inverter/gate-driver/W_GATE_H: track 40.4 -> 42.4 mm
- net /RP2350/RUN: track 24.6 -> 23.4 mm
